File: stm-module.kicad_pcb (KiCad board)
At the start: 2 copper layers, 45.2 x 59.1 mm, 40 parts, among them J1 Conn_01x05_Pin, J2 connectorL, J3 connectorR, J4 power, J5 USB_C_Receptacle_USB2.0_16P, SW1 Reset, U1 STM32G474RETx, U2 TPS7A20xxxDBV, Y1 Crystal

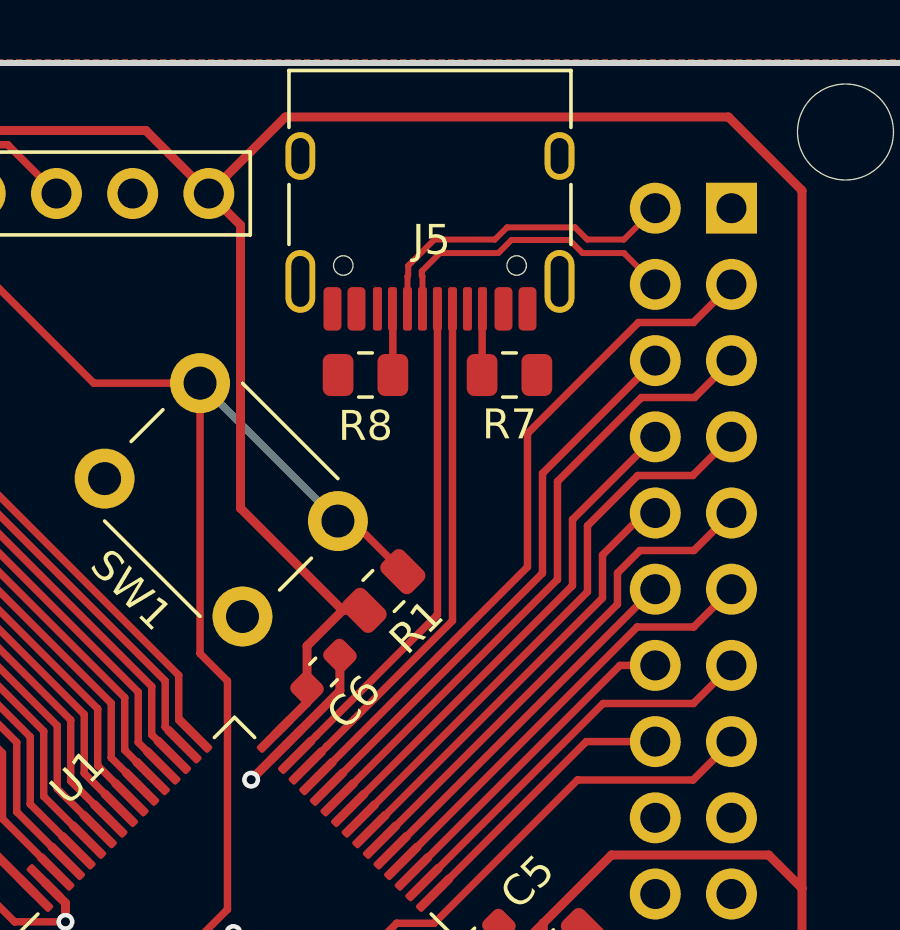
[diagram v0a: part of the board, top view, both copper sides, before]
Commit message: change usbc symbol
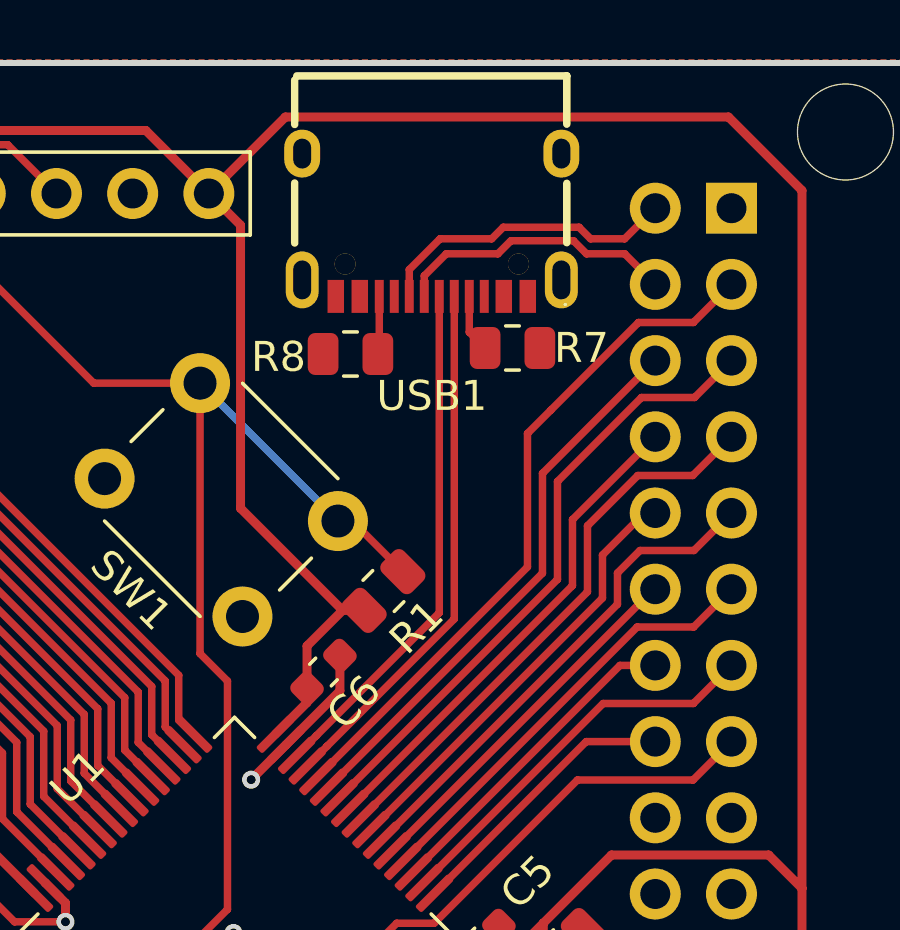
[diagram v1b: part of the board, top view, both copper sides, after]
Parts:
- removed J5: USB_C_Receptacle_USB2.0_16P, Connector_USB:USB_C_Receptacle_HRO_TYPE-C-31-M-12
- added USB1: TYPE-C 16PIN 2MD, EasyEDA:USB-C-SMD_TYPE-C-16PIN-2MD-073, F.Cu at (183.0, 102.4)
- moved R7 0.91 mm to (185.7, 106.5)
- moved R8 0.86 mm to (180.3, 106.7)

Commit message: pcb updates and gitignore update
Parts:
- removed REF** (x4): MountingHole_3.2mm_M3, MountingHole:MountingHole_3.2mm_M3
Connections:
- J3 pad 17: GND -> +3.3V
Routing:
- net /D-: track 27.2 -> 29.8 mm
- net /D+: track 27.5 -> 30.1 mm
- net +3.3V: track 299.0 -> 300.0 mm
